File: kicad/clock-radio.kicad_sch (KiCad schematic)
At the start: 46 parts, among them J1 Display Header, J2 Speaker Header, J3 USB_C_Receptacle_USB2.0_16P, J4 Rotary Encoder Header, J5 SWD Header, J6 Antenna, SW1 BOOT0, U1 STM32G0B1CETx, U2 PAM8302AAD, U3 MCP1700x-330xxTT, U4 DS3231MZ, U5 RDA5807M_Module, U6 USBLC6-2P6

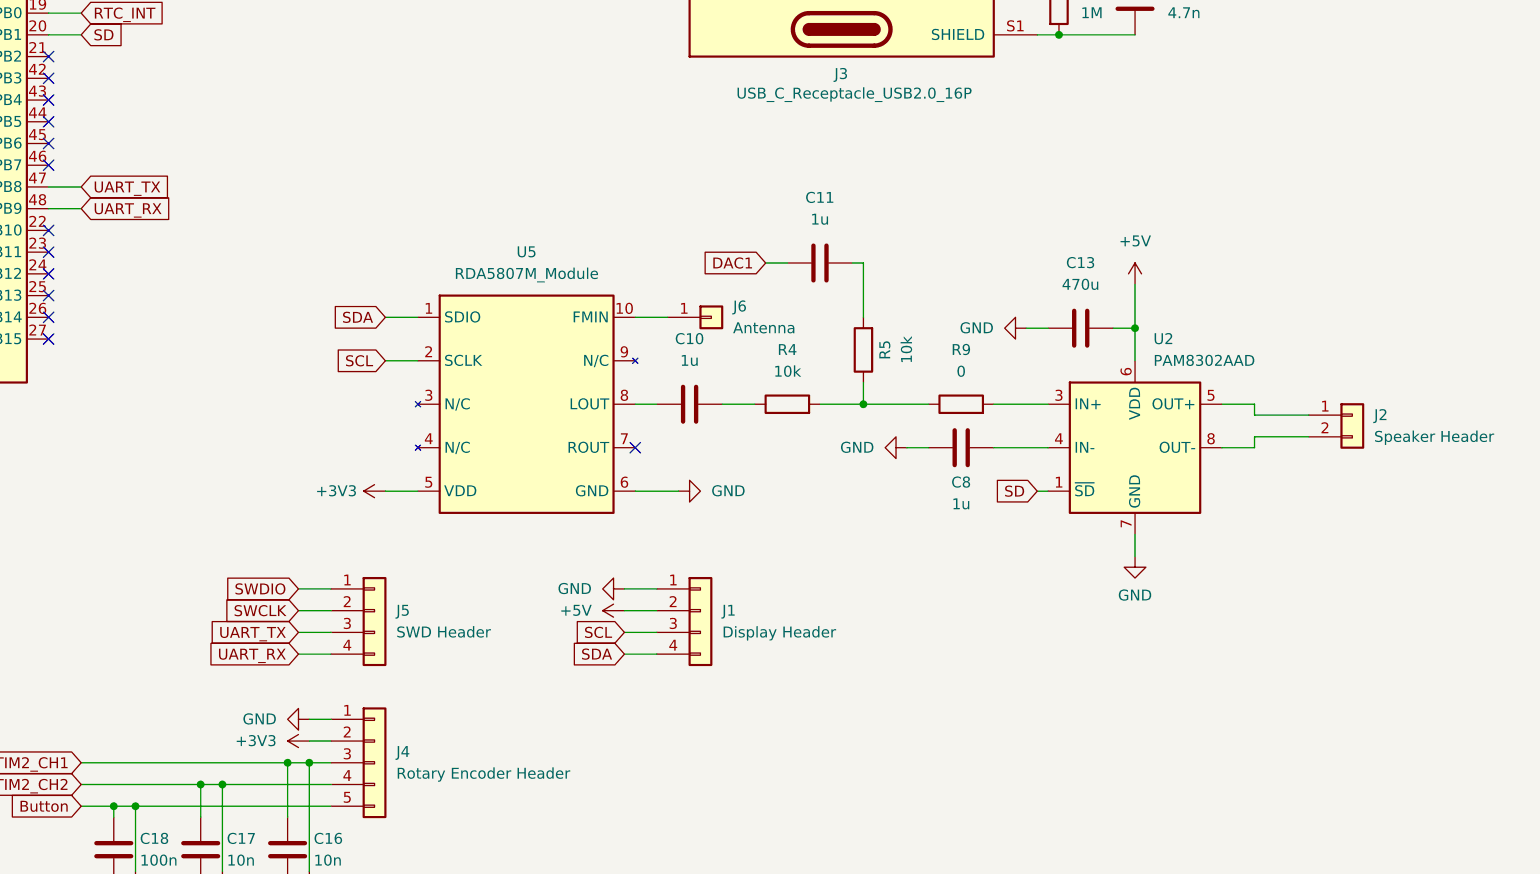
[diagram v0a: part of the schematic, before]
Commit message: Added decoupling capacitors and ferrite bead on radio module
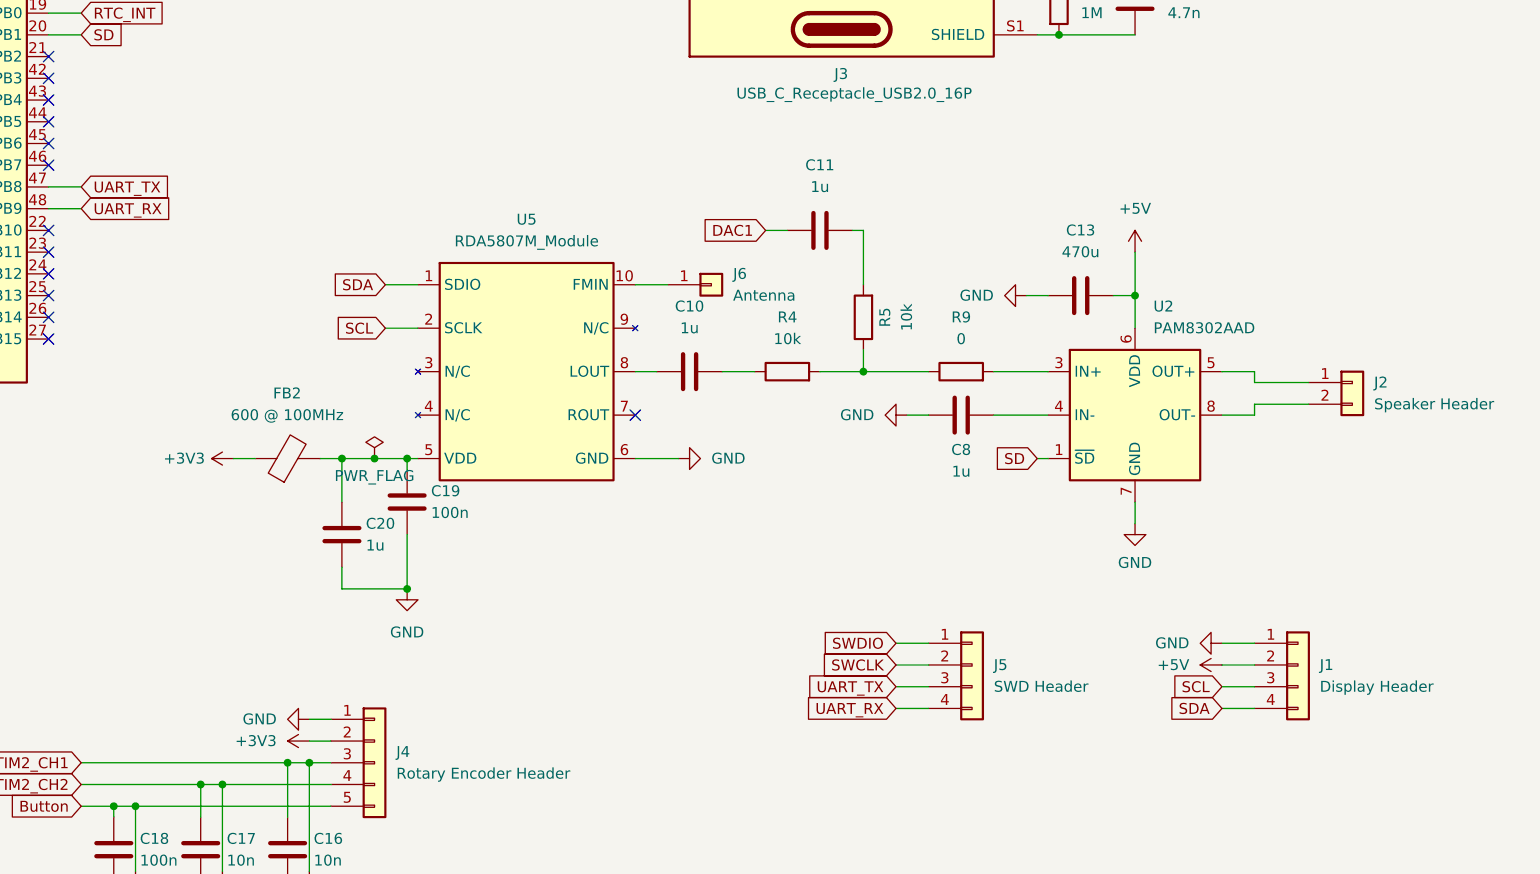
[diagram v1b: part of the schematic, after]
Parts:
- added C19: 100n, Capacitor_SMD:C_0402_1005Metric_Pad0.74x0.62mm_HandSolder, symbol Device:C
- added C20: 1u, Capacitor_SMD:C_0402_1005Metric_Pad0.74x0.62mm_HandSolder, symbol Device:C
- added FB2: 600 @ 100MHz, Capacitor_SMD:C_0603_1608Metric_Pad1.08x0.95mm_HandSolder, symbol Device:FerriteBead
- FB1: footprint (none) -> Capacitor_SMD:C_0603_1608Metric_Pad1.08x0.95mm_HandSolder
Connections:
- net +3V3: now also FB2.1; no longer U5.5 (VDD)
- net GND: now also C19.2, C20.2
- new net: C19.1, C20.1, FB2.2, U5.5 (VDD)
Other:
- moved on the sheet: C10, C11, C13, C8, J1, J2, J5, J6, R4, R5, R9, U2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

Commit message: started pcb design
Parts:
- C16: renamed from C8; footprint (none) -> Capacitor_SMD:C_0402_1005Metric_Pad0.74x0.62mm_HandSolder
- C20: renamed from C1; footprint (none) -> Capacitor_SMD:C_0402_1005Metric_Pad0.74x0.62mm_HandSolder
- J3: footprint (none) -> Connector_USB:USB_C_Receptacle_HCTL_HC-TYPE-C-16P-01A
- R1: renamed from R10; footprint (none) -> Resistor_SMD:R_0402_1005Metric_Pad0.72x0.64mm_HandSolder
- U6: renamed from U2; footprint (none) -> Package_SO:MSOP-8_3x3mm_P0.65mm
- renumbered C7 to C1, C20 to C10, C19 to C11, C15 to C12, C14 to C13, C10 to C14, C11 to C15, C3 to C17, C2 to C18, C13 to C19, C6 to C2, C9 to C3, C12 to C4, C4 to C5, C5 to C6, C18 to C7, C17 to C8, C16 to C9, J4 to J1, J6 to J2, J5 to J4, J1 to J5, J2 to J6, R4 to R10, R5 to R11, R9 to R12, R1 to R13, R8 to R2, R13 to R3, R7 to R4, R12 to R5, R11 to R7, R2 to R8, R3 to R9, U4 to U1, U1 to U2, U5 to U3, U3 to U4, U6 to U5

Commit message: updated pcb layout
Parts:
- R13, R8, R9: footprint Resistor_SMD:R_0201_0603Metric_Pad0.64x0.40mm_HandSolder -> Resistor_SMD:R_0402_1005Metric_Pad0.72x0.64mm_HandSolder
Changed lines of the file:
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@@
 			)
 		)
-		(property "Footprint" "Resistor_SMD:R_0201_0603Metric_Pad0.64x0.40mm_HandSolder"
+		(property "Footprint" "Resistor_SMD:R_0402_1005Metric_Pad0.72x0.64mm_HandSolder"
 			(at 226.822 77.47 90)
 			(effects
@@
 			)
 		)
-		(property "Footprint" "Resistor_SMD:R_0201_0603Metric_Pad0.64x0.40mm_HandSolder"
+		(property "Footprint" "Resistor_SMD:R_0402_1005Metric_Pad0.72x0.64mm_HandSolder"
 			(at 191.262 50.8 90)
 			(effects
@@
 			)
 		)
-		(property "Footprint" "Resistor_SMD:R_0201_0603Metric_Pad0.64x0.40mm_HandSolder"
+		(property "Footprint" "Resistor_SMD:R_0402_1005Metric_Pad0.72x0.64mm_HandSolder"
 			(at 193.802 43.18 90)
 			(effects

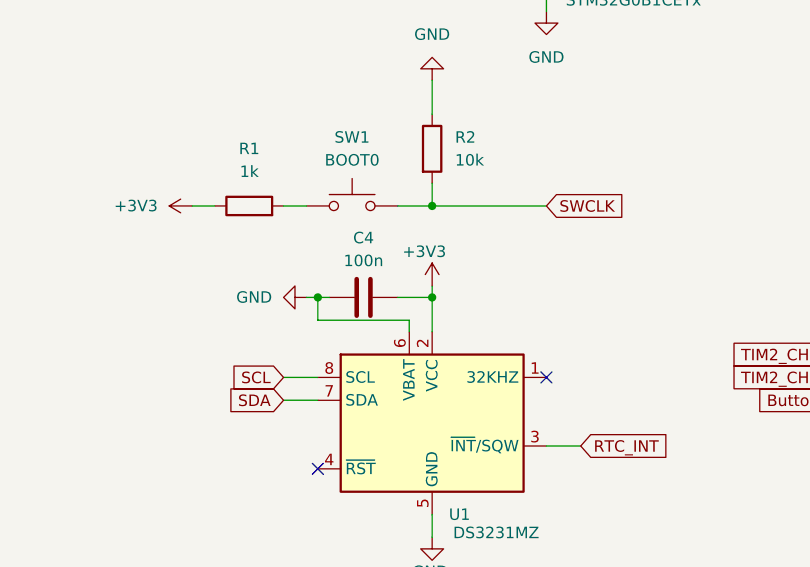
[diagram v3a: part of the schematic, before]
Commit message: added coin cell
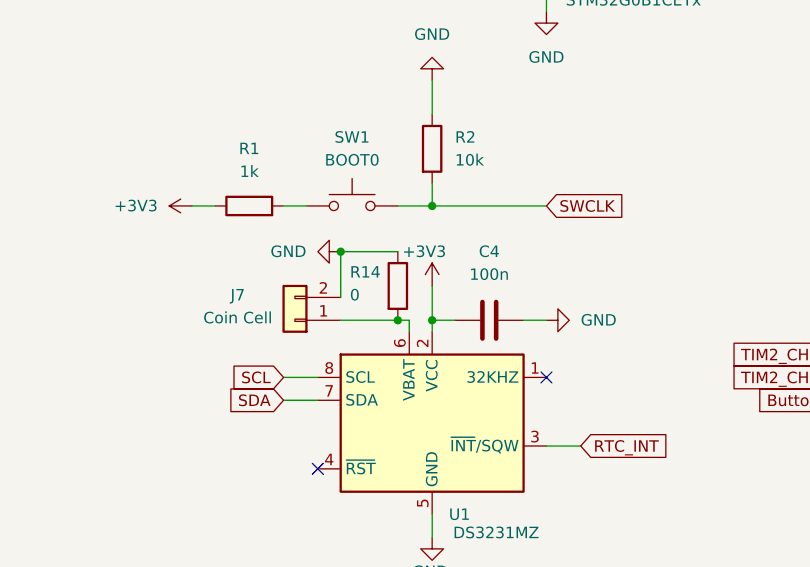
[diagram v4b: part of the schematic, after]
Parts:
- added J7: Coin Cell, Connector_PinSocket_2.54mm:PinSocket_1x02_P2.54mm_Vertical, symbol Connector_Generic:Conn_01x02
- added R14: 0, Resistor_SMD:R_0402_1005Metric_Pad0.72x0.64mm_HandSolder, symbol Device:R
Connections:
- net +3V3: now also C4.1; no longer C4.2
- net GND: now also C4.2, J7.2 (Pin_2), R14.1; no longer C4.1, U1.6 (VBAT)
- new net: J7.1 (Pin_1), R14.2, U1.6 (VBAT)

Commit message: connected all components and added in ground and power plane
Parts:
- J2: footprint Connector_Wire:SolderWire-2sqmm_1x01_D2mm_OD3.9mm -> Connector_Wire:SolderWire-0.5sqmm_1x01_D0.9mm_OD2.3mm
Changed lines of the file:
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@@
 		)
 		(instances
-			(project ""
+			(project "clock-radio"
 				(path "/34a5d594-0d7a-4eb1-974a-5ffec479d839"
 					(reference "FB1")
@@
 		)
 		(instances
-			(project ""
+			(project "clock-radio"
 				(path "/34a5d594-0d7a-4eb1-974a-5ffec479d839"
 					(reference "C4")
@@
 		)
 		(instances
-			(project ""
+			(project "clock-radio"
 				(path "/34a5d594-0d7a-4eb1-974a-5ffec479d839"
 					(reference "C5")
@@
 		)
 		(instances
-			(project ""
+			(project "clock-radio"
 				(path "/34a5d594-0d7a-4eb1-974a-5ffec479d839"
 					(reference "#FLG03")
@@
 		)
 		(instances
-			(project ""
+			(project "clock-radio"
 				(path "/34a5d594-0d7a-4eb1-974a-5ffec479d839"
 					(reference "R11")
@@
 		)
 		(instances
-			(project ""
+			(project "clock-radio"
 				(path "/34a5d594-0d7a-4eb1-974a-5ffec479d839"
 					(reference "#PWR09")
@@
 		)
 		(instances
-			(project ""
+			(project "clock-radio"
 				(path "/34a5d594-0d7a-4eb1-974a-5ffec479d839"
 					(reference "C9")
@@
 		)
 		(instances
-			(project ""
+			(project "clock-radio"
 				(path "/34a5d594-0d7a-4eb1-974a-5ffec479d839"
 					(reference "C14")
@@
 		)
 		(instances
-			(project ""
+			(project "clock-radio"
 				(path "/34a5d594-0d7a-4eb1-974a-5ffec479d839"
 					(reference "J6")
@@
 		)
 		(instances
-			(project ""
+			(project "clock-radio"
 				(path "/34a5d594-0d7a-4eb1-974a-5ffec479d839"
 					(reference "R10")
@@
 		)
 		(instances
-			(project ""
+			(project "clock-radio"
 				(path "/34a5d594-0d7a-4eb1-974a-5ffec479d839"
 					(reference "R6")
@@
 		)
 		(instances
-			(project ""
+			(project "clock-radio"
 				(path "/34a5d594-0d7a-4eb1-974a-5ffec479d839"
 					(reference "J1")
@@
 		)
 		(instances
-			(project ""
+			(project "clock-radio"
 				(path "/34a5d594-0d7a-4eb1-974a-5ffec479d839"
 					(reference "#PWR029")
@@
 		)
 		(instances
-			(project ""
+			(project "clock-radio"
 				(path "/34a5d594-0d7a-4eb1-974a-5ffec479d839"
 					(reference "#PWR018")
@@
 		)
 		(instances
-			(project ""
+			(project "clock-radio"
 				(path "/34a5d594-0d7a-4eb1-974a-5ffec479d839"
 					(reference "U2")
@@
 		)
 		(instances
-			(project ""
+			(project "clock-radio"
 				(path "/34a5d594-0d7a-4eb1-974a-5ffec479d839"
 					(reference "#PWR07")
@@
 		)
 		(instances
-			(project ""
+			(project "clock-radio"
 				(path "/34a5d594-0d7a-4eb1-974a-5ffec479d839"
 					(reference "#PWR015")
@@
 		)
 		(instances
-			(project ""
+			(project "clock-radio"
 				(path "/34a5d594-0d7a-4eb1-974a-5ffec479d839"
 					(reference "R12")
@@
 		)
 		(instances
-			(project ""
+			(project "clock-radio"
 				(path "/34a5d594-0d7a-4eb1-974a-5ffec479d839"
 					(reference "C11")
@@
 		)
 		(instances
-			(project ""
+			(project "clock-radio"
 				(path "/34a5d594-0d7a-4eb1-974a-5ffec479d839"
 					(reference "C13")
@@
 		)
 		(instances
-			(project ""
+			(project "clock-radio"
 				(path "/34a5d594-0d7a-4eb1-974a-5ffec479d839"
 					(reference "#PWR06")
@@
 		)
 		(instances
-			(project ""
+			(project "clock-radio"
 				(path "/34a5d594-0d7a-4eb1-974a-5ffec479d839"
 					(reference "U1")
@@
 		)
 		(instances
-			(project ""
+			(project "clock-radio"
 				(path "/34a5d594-0d7a-4eb1-974a-5ffec479d839"
 					(reference "C19")
@@
 		)
 		(instances
-			(project ""
+			(project "clock-radio"
 				(path "/34a5d594-0d7a-4eb1-974a-5ffec479d839"
 					(reference "U3")
@@
 		)
 		(instances
-			(project ""
+			(project "clock-radio"
 				(path "/34a5d594-0d7a-4eb1-974a-5ffec479d839"
 					(reference "#FLG01")
@@
 		)
 		(instances
-			(project ""
+			(project "clock-radio"
 				(path "/34a5d594-0d7a-4eb1-974a-5ffec479d839"
 					(reference "C16")
@@
 		)
 		(instances
-			(project ""
+			(project "clock-radio"
 				(path "/34a5d594-0d7a-4eb1-974a-5ffec479d839"
 					(reference "R14")
@@
 			)
 		)
-		(property "Footprint" "Connector_Wire:SolderWire-2sqmm_1x01_D2mm_OD3.9mm"
+		(property "Footprint" "Connector_Wire:SolderWire-0.5sqmm_1x01_D0.9mm_OD2.3mm"
 			(at 187.96 110.49 0)
 			(effects
@@
 		)
 		(instances
-			(project ""
+			(project "clock-radio"
 				(path "/34a5d594-0d7a-4eb1-974a-5ffec479d839"
 					(reference "J2")
@@
 		)
 		(instances
-			(project ""
+			(project "clock-radio"
 				(path "/34a5d594-0d7a-4eb1-974a-5ffec479d839"
 					(reference "R7")
@@
 		)
 		(instances
-			(project ""
+			(project "clock-radio"
 				(path "/34a5d594-0d7a-4eb1-974a-5ffec479d839"
 					(reference "#PWR03")
@@
 		)
 		(instances
-			(project ""
+			(project "clock-radio"
 				(path "/34a5d594-0d7a-4eb1-974a-5ffec479d839"
 					(reference "U6")

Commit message: swapped layers
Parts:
- J2: footprint Connector_Wire:SolderWire-0.5sqmm_1x01_D0.9mm_OD2.3mm -> Connector_Wire:SolderWire-0.75sqmm_1x01_D1.25mm_OD2.3mm
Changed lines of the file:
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@@
 			)
 		)
-		(property "Footprint" "Connector_Wire:SolderWire-0.5sqmm_1x01_D0.9mm_OD2.3mm"
+		(property "Footprint" "Connector_Wire:SolderWire-0.75sqmm_1x01_D1.25mm_OD2.3mm"
 			(at 187.96 110.49 0)
 			(effects

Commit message: updated cap
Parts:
- C19: value 470u -> 1u
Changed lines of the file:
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@@
 			)
 		)
-		(property "Value" "470u"
+		(property "Value" "1u"
 			(at 231.14 106.68 90)
 			(effects
